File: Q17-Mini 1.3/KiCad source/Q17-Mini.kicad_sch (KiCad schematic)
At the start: 86 parts, among them J1 INPUT, J2-1 SPK+, J2-2 SPK-, J3-1 V+, J3-2 GND, J3-3 V-, Q1 IRF610, Q10 KSA992, Q11 ZVP2106A, Q12 BD139, Q13 IRF610, Q14 IRF9610, Q15 FQA46N15, Q16 FQA36P15, Q2 KSA992, Q3 KSC1845, Q4 IRF9610, Q5 FQP3P20, Q6 FQP3N30, Q7 KSC1845, Q8 ZVN4206AV, Q9 ZVP2106A, U1 OPA1641

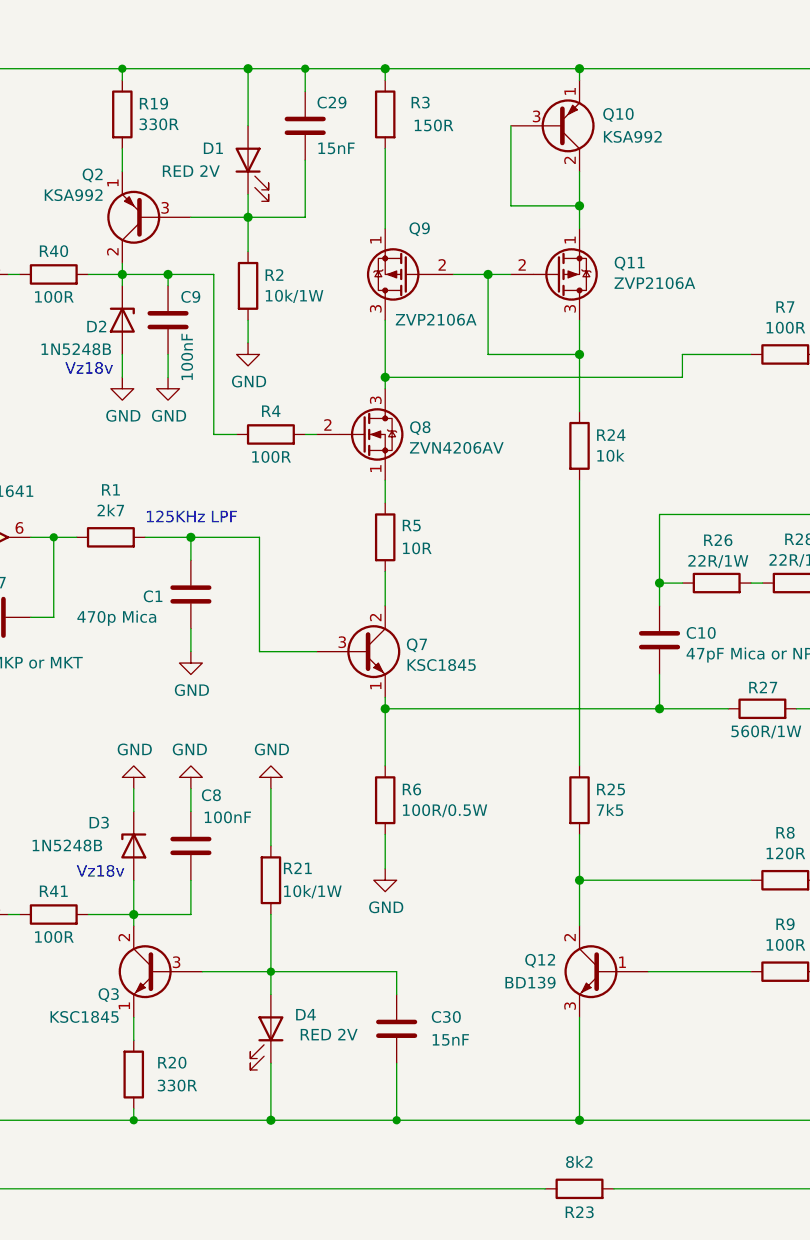
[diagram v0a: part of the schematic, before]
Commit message: Update README & diagram
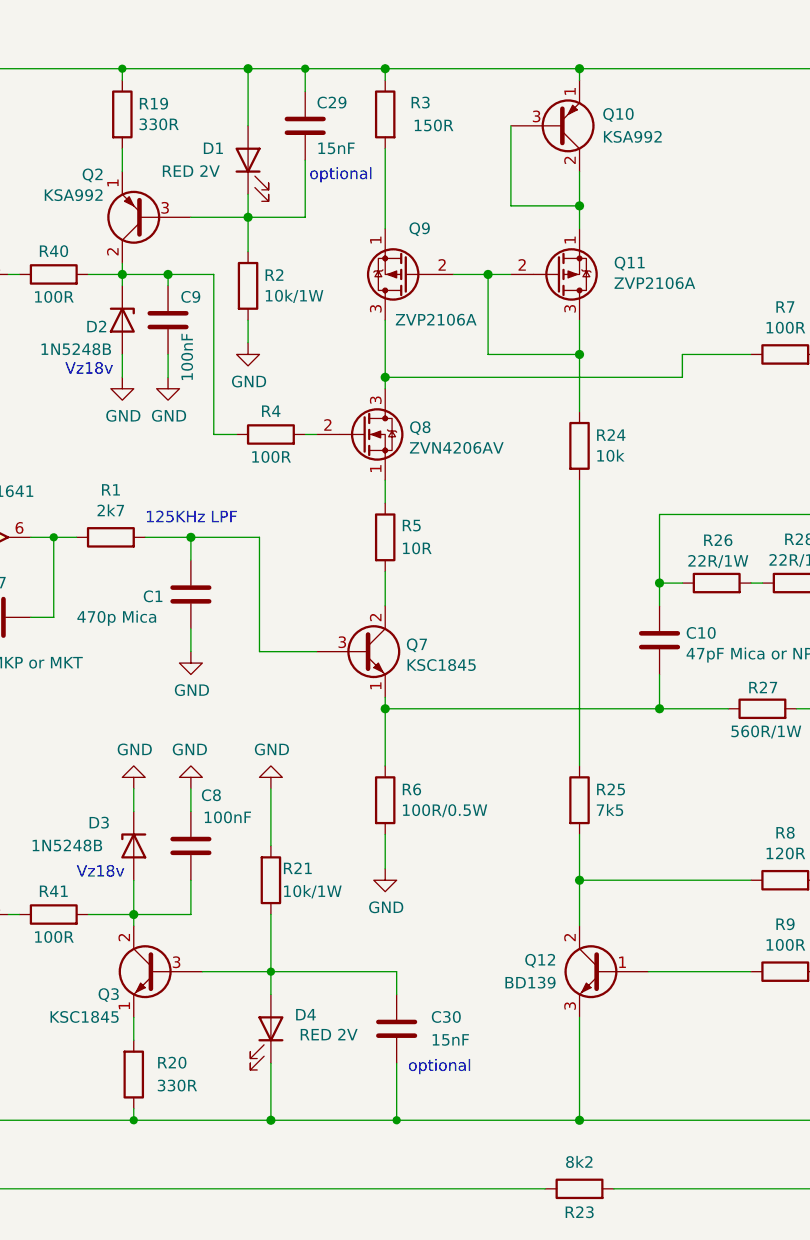
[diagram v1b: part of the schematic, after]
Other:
- note added: "optional"
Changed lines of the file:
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@@
   (title_block
     (title "Q17-Mini Amplifier")
-    (date "2022-09-07")
+    (date "2022-09-09")
     (rev "1.3.9")
     (company "by eng. Tiberiu Vicol")
@@
     (effects (font (size 1.27 1.27)) (justify left bottom))
   )
+  (text "optional" (at 110.9491 36.8038 0)
+    (effects (font (size 1.27 1.27)) (justify left bottom))
+  )
   (text "125KHz LPF" (at 92.71 74.93 0)
     (effects (font (size 1.27 1.27)) (justify left bottom))
@@
     (effects (font (size 1.27 1.27)) (justify left bottom))
   )
+  (text "optional" (at 121.92 135.89 0)
+    (effects (font (size 1.27 1.27)) (justify left bottom))
+  )

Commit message: Upgraded Q17-Mini 1.3
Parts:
- C3, C6: value 100uF/16V -> 47uF/25v; Part# RFS-16V101MH3#5 -> Nichicon Muse UKZ1E470MPM
- U1: value OPA1641 -> OPA1611; Part# OPA1641AID -> OPA1611AID
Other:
- note added: "C3, C6 : Nichicon UKZ1E470MPM"
- note removed: "C3, C6 : ELna Silmic II 100uF 16v"
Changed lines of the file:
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@@
   (title_block
     (title "Q17-Mini Amplifier")
-    (date "2022-09-09")
+    (date "2022-09-11")
     (rev "1.3.9")
     (company "by eng. Tiberiu Vicol")
@@
     (effects (font (size 1.27 1.27)) (justify left bottom))
   )
-  (text "C3, C6 : ELna Silmic II 100uF 16v" (at 59.69 179.07 0)
+  (text "C3, C6 : Nichicon UKZ1E470MPM" (at 59.69 179.07 0)
     (effects (font (size 1.27 1.27)) (justify left bottom))
   )
@@
     (in_bom yes) (on_board yes)
     (property "Reference" "C6" (id 0) (at 60.4721 105.363 90))
-    (property "Value" "100uF/16V" (id 1) (at 62.484 112.776 90))
+    (property "Value" "47uF/25v" (id 1) (at 62.484 112.776 90))
     (property "Footprint" "Capacitor_THT:CP_Radial_D10.0mm_P5.00mm" (id 2) (at 67.31 106.9848 0)
       (effects (font (size 1.27 1.27)) hide)
@@
       (effects (font (size 1.27 1.27)) hide)
     )
-    (property "Part#" "RFS-16V101MH3#5" (id 4) (at 63.5 107.95 90)
+    (property "Part#" "Nichicon Muse UKZ1E470MPM" (id 4) (at 63.5 107.95 90)
       (effects (font (size 1.27 1.27)) hide)
     )
@@
     (in_bom yes) (on_board yes)
     (property "Reference" "C3" (id 0) (at 63.754 50.8 90))
-    (property "Value" "100uF/16V" (id 1) (at 63.754 53.0987 90))
+    (property "Value" "47uF/25v" (id 1) (at 63.754 53.0987 90))
     (property "Footprint" "Capacitor_THT:CP_Radial_D10.0mm_P5.00mm" (id 2) (at 59.69 58.1152 0)
       (effects (font (size 1.27 1.27)) hide)
@@
       (effects (font (size 1.27 1.27)) hide)
     )
-    (property "Part#" "RFS-16V101MH3#5" (id 4) (at 63.5 57.15 90)
+    (property "Part#" "Nichicon Muse UKZ1E470MPM" (id 4) (at 63.5 57.15 90)
       (effects (font (size 1.27 1.27)) hide)
     )
@@
       (effects (font (size 1.27 1.27)) (justify left))
     )
-    (property "Value" "OPA1641" (id 1) (at 72.39 71.12 0)
+    (property "Value" "OPA1611" (id 1) (at 72.39 71.12 0)
       (effects (font (size 1.27 1.27)) (justify left))
     )
@@
       (effects (font (size 1.27 1.27)) hide)
     )
-    (property "Part#" "OPA1641AID" (id 4) (at 72.39 76.2 0)
+    (property "Part#" "OPA1611AID" (id 4) (at 72.39 76.2 0)
       (effects (font (size 1.27 1.27)) hide)
     )
@@
     )
     (path "/a873e942-d614-4558-aa34-f59b59912653"
-      (reference "C3") (unit 1) (value "100uF/16V") (footprint "Capacitor_THT:CP_Radial_D10.0mm_P5.00mm")
+      (reference "C3") (unit 1) (value "47uF/25v") (footprint "Capacitor_THT:CP_Radial_D10.0mm_P5.00mm")
     )
     (path "/ec41bd13-d169-4b04-82e8-82bf8614a606"
@@
     )
     (path "/36992cac-f26a-4454-857c-961531074fa8"
-      (reference "C6") (unit 1) (value "100uF/16V") (footprint "Capacitor_THT:CP_Radial_D10.0mm_P5.00mm")
+      (reference "C6") (unit 1) (value "47uF/25v") (footprint "Capacitor_THT:CP_Radial_D10.0mm_P5.00mm")
     )
     (path "/87fb4618-ffba-4098-894c-2a108e97e5a6"
@@
     )
     (path "/d3ffbaf8-6b20-4c43-96f7-9b88cf0a305f"
-      (reference "U1") (unit 1) (value "OPA1641") (footprint "Package_SO:SOIC-8_3.9x4.9mm_P1.27mm")
+      (reference "U1") (unit 1) (value "OPA1611") (footprint "Package_SO:SOIC-8_3.9x4.9mm_P1.27mm")
     )
   )

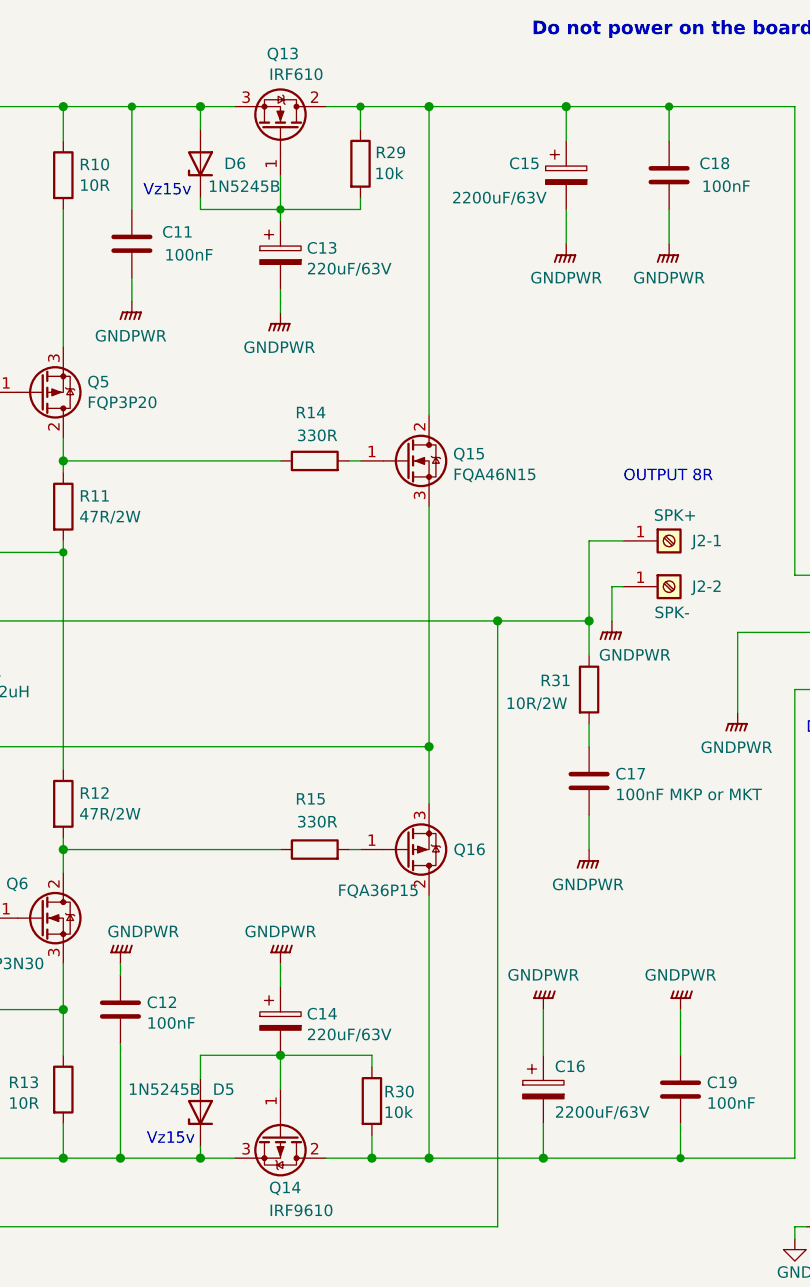
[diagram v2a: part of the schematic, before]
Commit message: Update diagram for Q17-Mini 1.3
Changed R29/R30 to 100R.
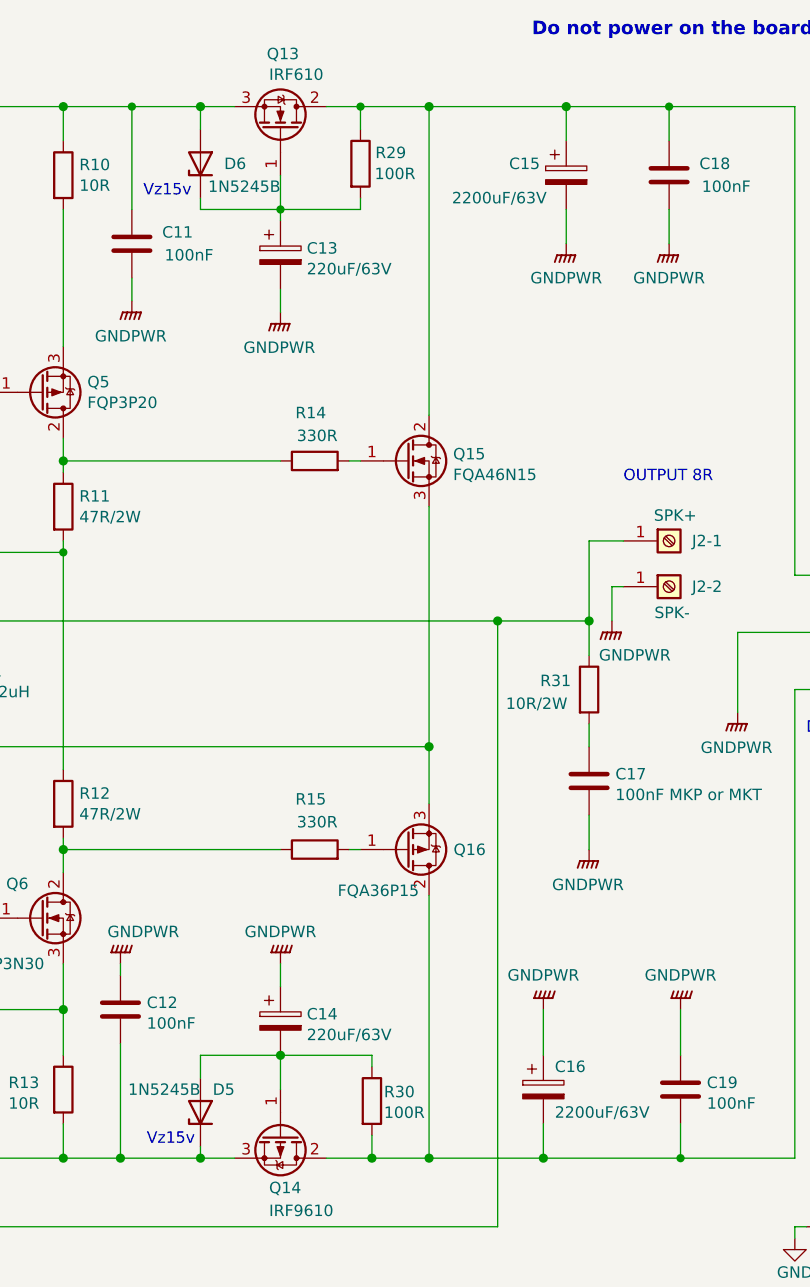
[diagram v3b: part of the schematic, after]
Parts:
- R29, R30: value 10k -> 100R; Part# MRS25000C1002FCT00 -> MRS25000C1000FC100
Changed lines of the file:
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@@
   (title_block
     (title "Q17-Mini Amplifier")
-    (date "2022-09-11")
+    (date "2022-09-13")
     (rev "1.3.9")
     (company "by eng. Tiberiu Vicol")
@@
       (effects (font (size 1.27 1.27)) (justify left))
     )
-    (property "Value" "10k" (id 1) (at 216.2005 31.5986 0)
+    (property "Value" "100R" (id 1) (at 216.2005 31.5986 0)
       (effects (font (size 1.27 1.27)) (justify left))
     )
@@
       (effects (font (size 1.27 1.27)) hide)
     )
-    (property "Part#" "MRS25000C1002FCT00" (id 4) (at 214.63 30.48 0)
+    (property "Part#" "MRS25000C1000FC100" (id 4) (at 214.63 30.48 0)
       (effects (font (size 1.27 1.27)) hide)
     )
@@
       (effects (font (size 1.27 1.27)) (justify left))
     )
-    (property "Value" "10k" (id 1) (at 217.2359 135.9102 0)
+    (property "Value" "100R" (id 1) (at 217.2359 135.9102 0)
       (effects (font (size 1.27 1.27)) (justify left))
     )
@@
       (effects (font (size 1.27 1.27)) hide)
     )
-    (property "Part#" "MRS25000C1002FCT00" (id 4) (at 215.9 134.62 0)
+    (property "Part#" "MRS25000C1000FC100" (id 4) (at 215.9 134.62 0)
       (effects (font (size 1.27 1.27)) hide)
     )
@@
     )
     (path "/6a502bca-5c03-4909-9915-ce87906e504a"
-      (reference "R29") (unit 1) (value "10k") (footprint "Resistor_THT:R_Axial_DIN0207_L6.3mm_D2.5mm_P10.16mm_Horizontal")
+      (reference "R29") (unit 1) (value "100R") (footprint "Resistor_THT:R_Axial_DIN0207_L6.3mm_D2.5mm_P10.16mm_Horizontal")
     )
     (path "/860cc2f6-176f-4935-b38a-f52437fa5513"
-      (reference "R30") (unit 1) (value "10k") (footprint "Resistor_THT:R_Axial_DIN0207_L6.3mm_D2.5mm_P10.16mm_Horizontal")
+      (reference "R30") (unit 1) (value "100R") (footprint "Resistor_THT:R_Axial_DIN0207_L6.3mm_D2.5mm_P10.16mm_Horizontal")
     )
     (path "/0b38258b-fc2c-4616-935a-ea7f37c299ab"

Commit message: Update Q17-Mini.kicad_sch
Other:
- note added: "Q5, Q15, Q6, Q16 and Q20 need film Insulator and insulating washer spacer."
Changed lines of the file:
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@@
   (title_block
     (title "Q17-Mini Amplifier")
-    (date "2022-09-13")
+    (date "2022-09-25")
     (rev "1.3.9")
     (company "by eng. Tiberiu Vicol")
@@
     (effects (font (size 1.27 1.27)) (justify left bottom))
   )
+  (text "Q5, Q15, Q6, Q16 and Q20 need film Insulator and insulating washer spacer."
+    (at 96.52 163.83 0)
+    (effects (font (size 1.27 1.27)) (justify left bottom))
+  )
